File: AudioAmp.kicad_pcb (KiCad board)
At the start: 2 copper layers, 145 x 40 mm, 59 parts, among them J1 ACJS-MHOM, J2 ACJS-MHOM, Q1 MJE182G, Q12 MMBT5401, Q13 MMBT5401, Q2 MJE172G, Q3 MMBT5551(RANGE:200-300), Q9 MMBT5551(RANGE:200-300)

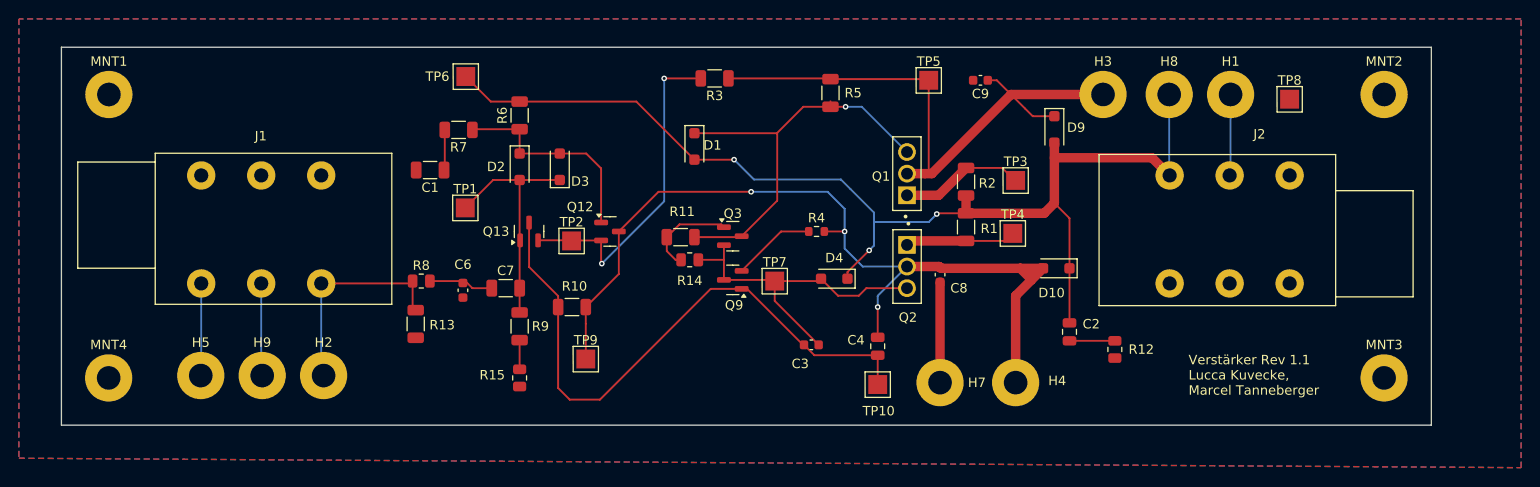
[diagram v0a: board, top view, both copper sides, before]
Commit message: CHA: Silkscreen Beschriftungen nun lesbar statt nummeriert
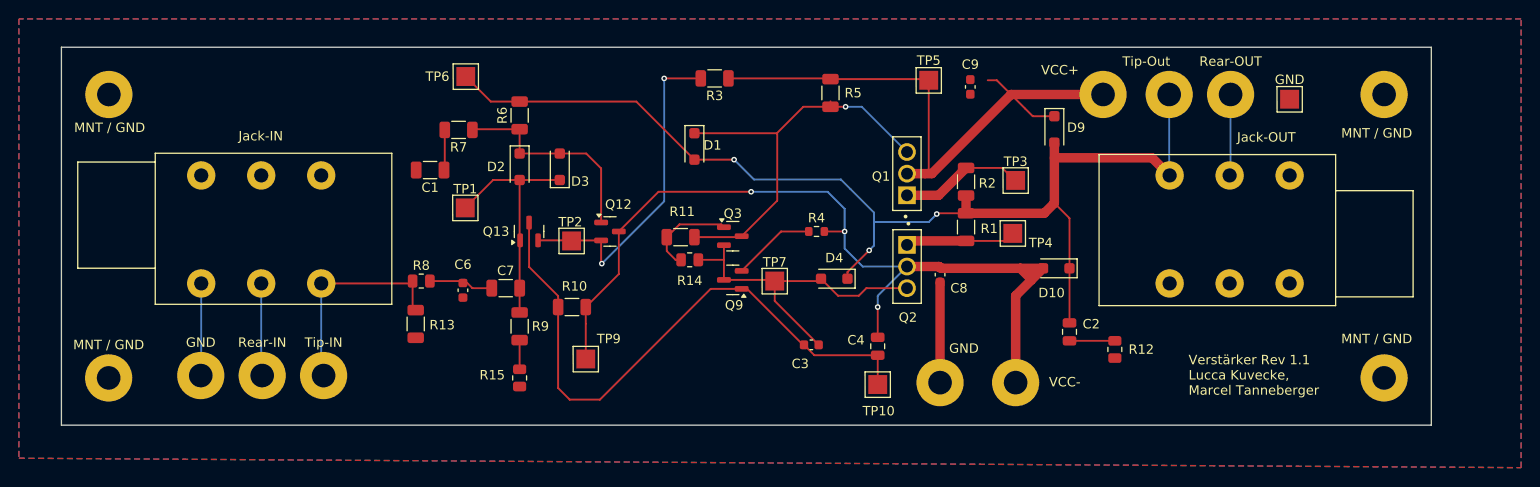
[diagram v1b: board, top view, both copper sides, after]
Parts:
- MNT / GND: renamed from MNT4
- MNT / GND: renamed from MNT3
- MNT / GND: renamed from MNT2
- MNT / GND: renamed from MNT1
- moved C9 1.28 mm to (161.2, 91.7), turned to 90 degrees
- renumbered H5 to GND, H7 to GND, TP8 to GND, J1 to Jack-IN, J2 to Jack-OUT, H9 to Rear-IN, H1 to Rear-OUT, H2 to Tip-IN, H8 to Tip-Out, H3 to VCC+, H4 to VCC-
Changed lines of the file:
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@@
 		(descr "Mounting Hole 2.5mm")
 		(tags "mounting hole 2.5mm")
-		(property "Reference" "MNT4"
+		(property "Reference" "MNT / GND"
 			(at 0 -3.5 0)
 			(layer "F.SilkS")
@@
 		(descr "Mounting Hole 2.5mm")
 		(tags "mounting hole 2.5mm")
-		(property "Reference" "H3"
-			(at 0 -3.5 0)
+		(property "Reference" "VCC+"
+			(at -4.562 -2.584 0)
 			(layer "F.SilkS")
 			(effects
@@
 		(tags "test point SMD pad rectangle square")
 		(property "Reference" "TP9"
-			(at 0 -1.998 0)
+			(at 2.436 -2.136 0)
 			(layer "F.SilkS")
 			(effects
@@
 		(descr "Mounting Hole 2.5mm")
 		(tags "mounting hole 2.5mm")
-		(property "Reference" "H8"
-			(at 0 -3.5 0)
+		(property "Reference" "Tip-Out"
+			(at -2.418 -3.5 0)
 			(layer "F.SilkS")
 			(effects
@@
 		(descr "Mounting Hole 2.5mm")
 		(tags "mounting hole 2.5mm")
-		(property "Reference" "H4"
-			(at 4.4 -0.2 0)
+		(property "Reference" "VCC-"
+			(at 5.196 -0.064 0)
 			(layer "F.SilkS")
 			(effects
@@
 		(descr "Mounting Hole 2.5mm")
 		(tags "mounting hole 2.5mm")
-		(property "Reference" "H1"
+		(property "Reference" "Rear-OUT"
 			(at 0 -3.5 0)
 			(layer "F.SilkS")
@@
 		(tags "SOT TO_SOT_SMD")
 		(property "Reference" "Q12"
-			(at -3.1625 -2.6 0)
+			(at 0.8895 -2.86 0)
 			(layer "F.SilkS")
 			(effects
@@
 		(descr "Mounting Hole 2.5mm")
 		(tags "mounting hole 2.5mm")
-		(property "Reference" "MNT3"
-			(at 0 -3.5 0)
+		(property "Reference" "MNT / GND"
+			(at -0.784 -4.136 0)
 			(layer "F.SilkS")
 			(effects
@@
 		(tags "test point SMD pad rectangle square")
 		(property "Reference" "TP4"
-			(at 0 -1.998 0)
+			(at 2.956 1.004 0)
 			(layer "F.SilkS")
 			(effects
@@
 		(descr "Mounting Hole 2.5mm")
 		(tags "mounting hole 2.5mm")
-		(property "Reference" "H5"
+		(property "Reference" "GND"
 			(at 0 -3.5 0)
 			(layer "F.SilkS")
@@
 		(descr "Mounting Hole 2.5mm")
 		(tags "mounting hole 2.5mm")
-		(property "Reference" "H2"
+		(property "Reference" "Tip-IN"
 			(at 0 -3.5 0)
 			(layer "F.SilkS")
@@
 		(descr "Mounting Hole 2.5mm")
 		(tags "mounting hole 2.5mm")
-		(property "Reference" "MNT2"
-			(at 0 -3.5 0)
+		(property "Reference" "MNT / GND"
+			(at -0.784 3.512 0)
 			(layer "F.SilkS")
 			(effects
@@
 					(thickness 0.15)
 				)
+				(justify top)
 			)
 		)
@@
 		(descr "Mounting Hole 2.5mm")
 		(tags "mounting hole 2.5mm")
-		(property "Reference" "H7"
-			(at 3.9 0 0)
+		(property "Reference" "GND"
+			(at 2.528 -3.62 0)
 			(layer "F.SilkS")
 			(effects
@@
 	(footprint "Capacitor_SMD:C_0603_1608Metric"
 		(layer "F.Cu")
-		(at 162.275 91 180)
+		(at 161.2 91.7 90)
 		(descr "Capacitor SMD 0603 (1608 Metric), square (rectangular) end terminal, IPC-7351 nominal, (Body size source: IPC-SM-782 page 76, https://www.pcb-3d.com/wordpress/wp-content/uploads/ipc-sm-782a_amendment_1_and_2.pdf), generated with kicad-footprint-generator")
 		(tags "capacitor")
 		(property "Reference" "C9"
-			(at 0 -1.43 0)
+			(at 2.375 0 180)
 			(layer "F.SilkS")
 			(effects
@@
 		)
 		(property "Value" "100n"
-			(at 0 1.43 0)
+			(at 0 1.43 90)
 			(layer "F.Fab")
 			(effects
@@
 		)
 		(property "Datasheet" "https://www.lcsc.com/datasheet/lcsc_datasheet_2211101700_YAGEO-CC0603KRX7R9BB104_C14663.pdf"
-			(at 0 0 0)
+			(at 0 0 90)
 			(layer "F.Fab")
 			(hide yes)
@@
 		)
 		(property "Description" "50V 100nF X7R ±10% 0603 Multilayer Ceramic Capacitors MLCC - SMD/SMT ROHS"
-			(at 0 0 0)
+			(at 0 0 90)
 			(layer "F.Fab")
 			(hide yes)
@@
 		)
 		(property "MPN" "C14663"
-			(at 0 0 180)
+			(at 0 0 90)
 			(unlocked yes)
 			(layer "F.Fab")
@@
 		(descr "Mounting Hole 2.5mm")
 		(tags "mounting hole 2.5mm")
-		(property "Reference" "H9"
+		(property "Reference" "Rear-IN"
 			(at 0 -3.5 0)
 			(layer "F.SilkS")
@@
 		(descr "Mounting Hole 2.5mm")
 		(tags "mounting hole 2.5mm")
-		(property "Reference" "MNT1"
-			(at 0 -3.5 0)
+		(property "Reference" "MNT / GND"
+			(at 0.08 3.509 0)
 			(layer "F.SilkS")
 			(effects
@@
 		(tags "test point SMD pad rectangle square")
 		(property "Reference" "TP5"
-			(at 0 -1.998 0)
+			(at 0 -2.1 0)
 			(layer "F.SilkS")
 			(effects
@@
 		(descr "Slim Jacks, 6.35mm (1/4in) stereo jack, metal nose with efficient chassis ground connection, T+R+S normalling contact, https://www.neutrik.com/en/product/nrj6hm-1")
 		(tags "neutrik jack slim")
-		(property "Reference" "J2"
-			(at 9.5 -4.37 0)
+		(property "Reference" "Jack-OUT"
+			(at 10.232 -4.042 0)
 			(layer "F.SilkS")
 			(effects
@@
 		(descr "SMD rectangular pad as test Point, square 2.0mm side length")
 		(tags "test point SMD pad rectangle square")
-		(property "Reference" "TP8"
-			(at 0 -1.998 0)
+		(property "Reference" "GND"
+			(at 0 -2.068 0)
 			(layer "F.SilkS")
 			(effects
@@
 		(tags "test point SMD pad rectangle square")
 		(property "Reference" "TP2"
-			(at 0 -1.998 0)
+			(at -0.128 -1.998 0)
 			(layer "F.SilkS")
 			(effects
@@
 		(descr "Slim Jacks, 6.35mm (1/4in) stereo jack, metal nose with efficient chassis ground connection, T+R+S normalling contact, https://www.neutrik.com/en/product/nrj6hm-1")
 		(tags "neutrik jack slim")
-		(property "Reference" "J1"
+		(property "Reference" "Jack-IN"
 			(at 6.4 15.6 0)
 			(layer "F.SilkS")

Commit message: CHA: Optimierungen in Leiterbahnen
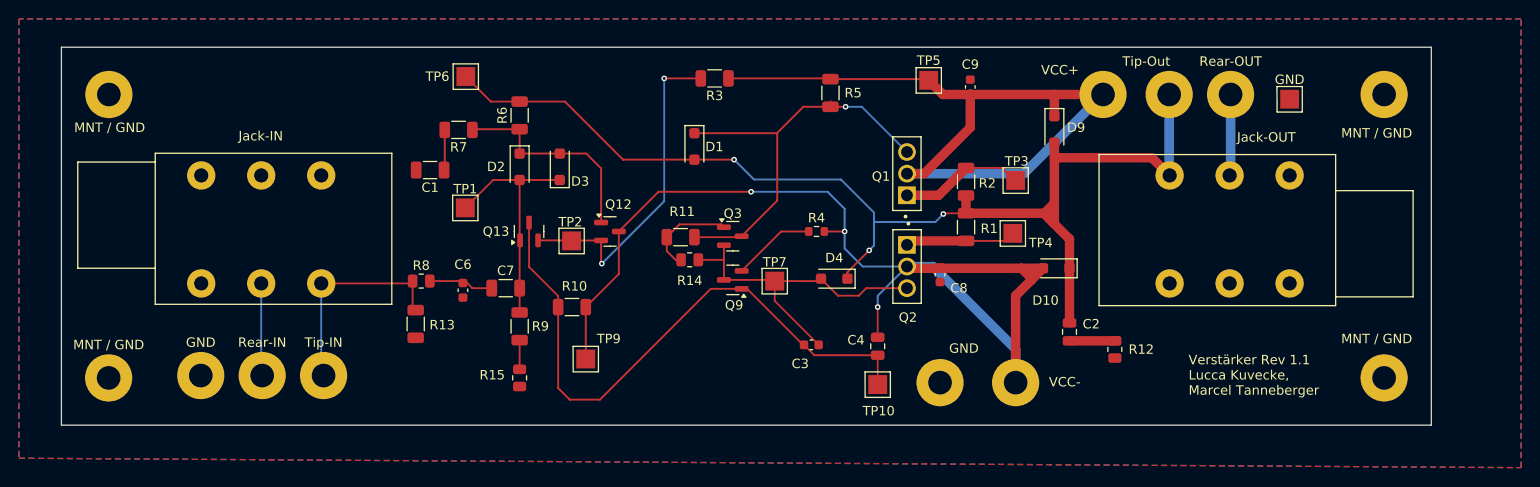
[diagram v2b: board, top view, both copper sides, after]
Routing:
- net /GND: track 20.4 -> 0.07 mm
- net Net-(D10-A): track 93.8 -> 112.5 mm
- net Net-(D9-K): track 64.2 -> 79.0 mm
- net Net-(D1-A): track 120.4 -> 122.0 mm

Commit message: CHA: Syncronität SHA / PCB
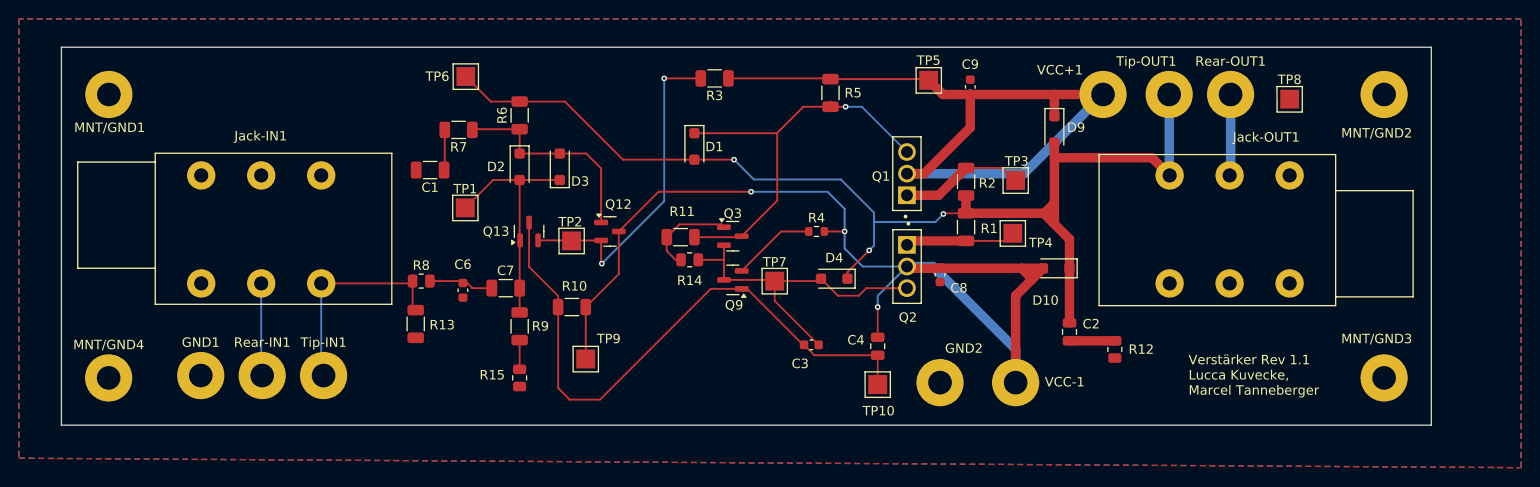
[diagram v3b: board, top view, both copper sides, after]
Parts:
- MNT/GND1, MNT/GND2, MNT/GND3, MNT/GND4: renamed from MNT / GND
- renumbered GND to GND1, GND to GND2, Jack-IN to Jack-IN1, Jack-OUT to Jack-OUT1, Rear-IN to Rear-IN1, Rear-OUT to Rear-OUT1, GND to TP8, Tip-IN to Tip-IN1, Tip-Out to Tip-OUT1, VCC+ to VCC+1, VCC- to VCC-1
